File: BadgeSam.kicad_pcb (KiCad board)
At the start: 2 copper layers, 50.1 x 32.4 mm, 2 parts

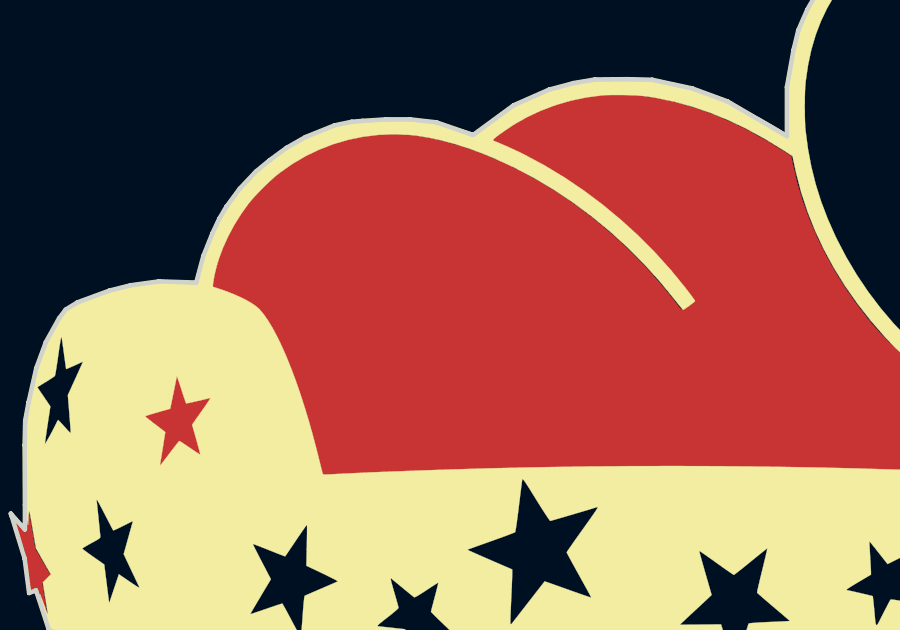
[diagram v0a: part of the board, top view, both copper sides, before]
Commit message: add logo wurth
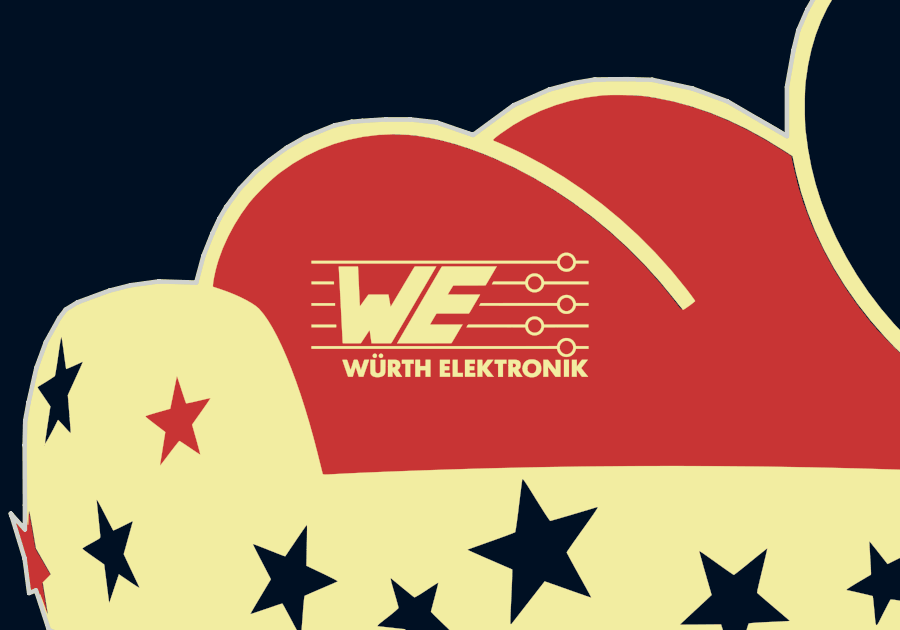
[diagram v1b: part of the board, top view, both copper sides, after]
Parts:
- added G***: LOGO, Aesthetics:wurth_4x4, F.Cu at (132.1, 103.4)

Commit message: define size
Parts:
- added BT1: Battery_Cell, BadgeSam:79523141, B.Cu at (138.9, 117.3)
- added C1: 1uF, Capacitor_SMD:C_0805_2012Metric_Pad1.15x1.40mm_HandSolder, B.Cu at (153.2, 133.3)
- added C2: 0.1uF, Capacitor_SMD:C_0805_2012Metric_Pad1.15x1.40mm_HandSolder, B.Cu at (168.1, 131.3)
- added D1: LED_RGBA, BadgeSam:LED_155124M173200, B.Cu at (118.6, 119.6)
- added D2: LED_RGBA, BadgeSam:LED_155124M173200, B.Cu at (164.3, 97.1)
- added D3: LED_RGBA, BadgeSam:LED_155124M173200, B.Cu at (129.2, 132.4)
- added D4: LED_RGBA, BadgeSam:LED_155124M173200, B.Cu at (153.9, 101.3)
- added R1: 10K, Resistor_SMD:R_0805_2012Metric_Pad1.15x1.40mm_HandSolder, B.Cu at (167.1, 124.0)
- added SW1: RESET, Button_Switch_SMD:SW_SPST_TL3342, B.Cu at (175.6, 114.2)
- added U1: STM8S003F3P, Package_SO:TSSOP-20_4.4x6.5mm_P0.65mm, B.Cu at (160.0, 128.0)
- moved Ref** 106.9 mm to (148.4, 112.4)
- moved G*** 9.26 mm to (130.6, 112.5)
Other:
- board outline removed

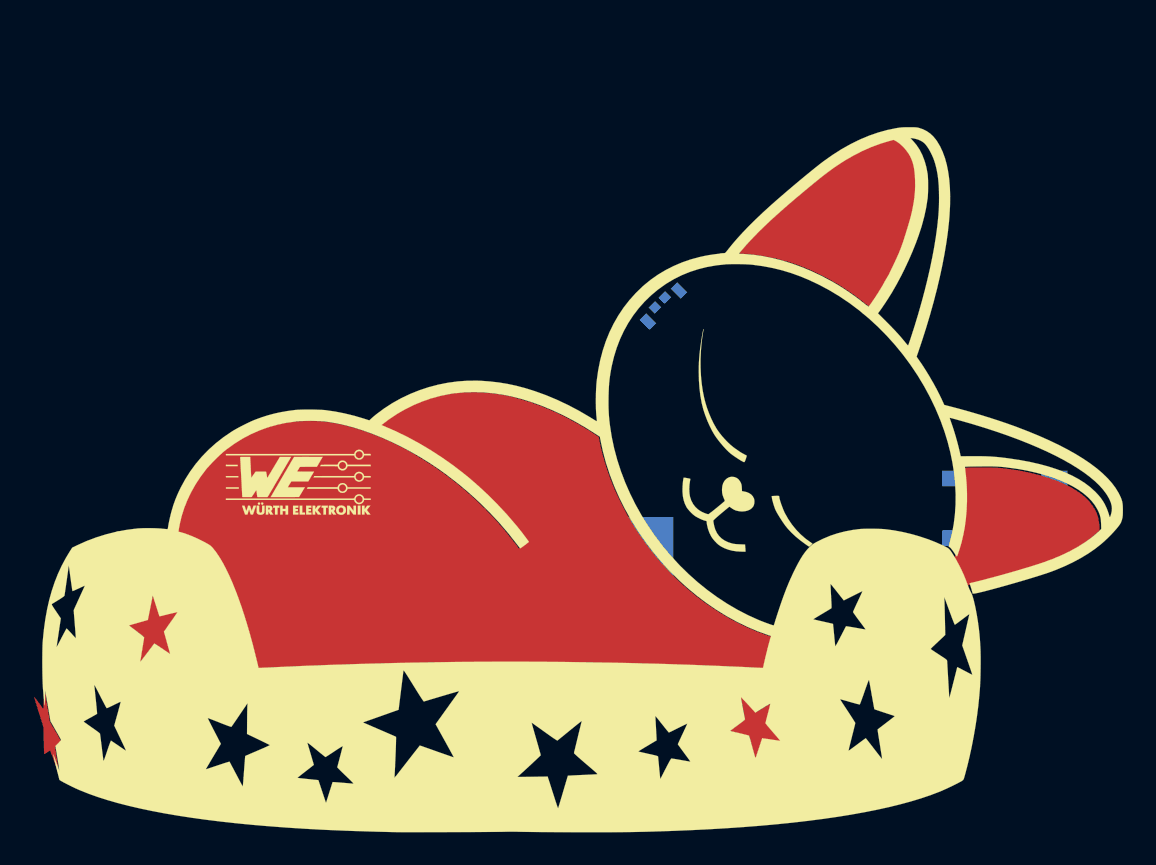
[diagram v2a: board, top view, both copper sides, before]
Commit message: Add EdgeCut and logos
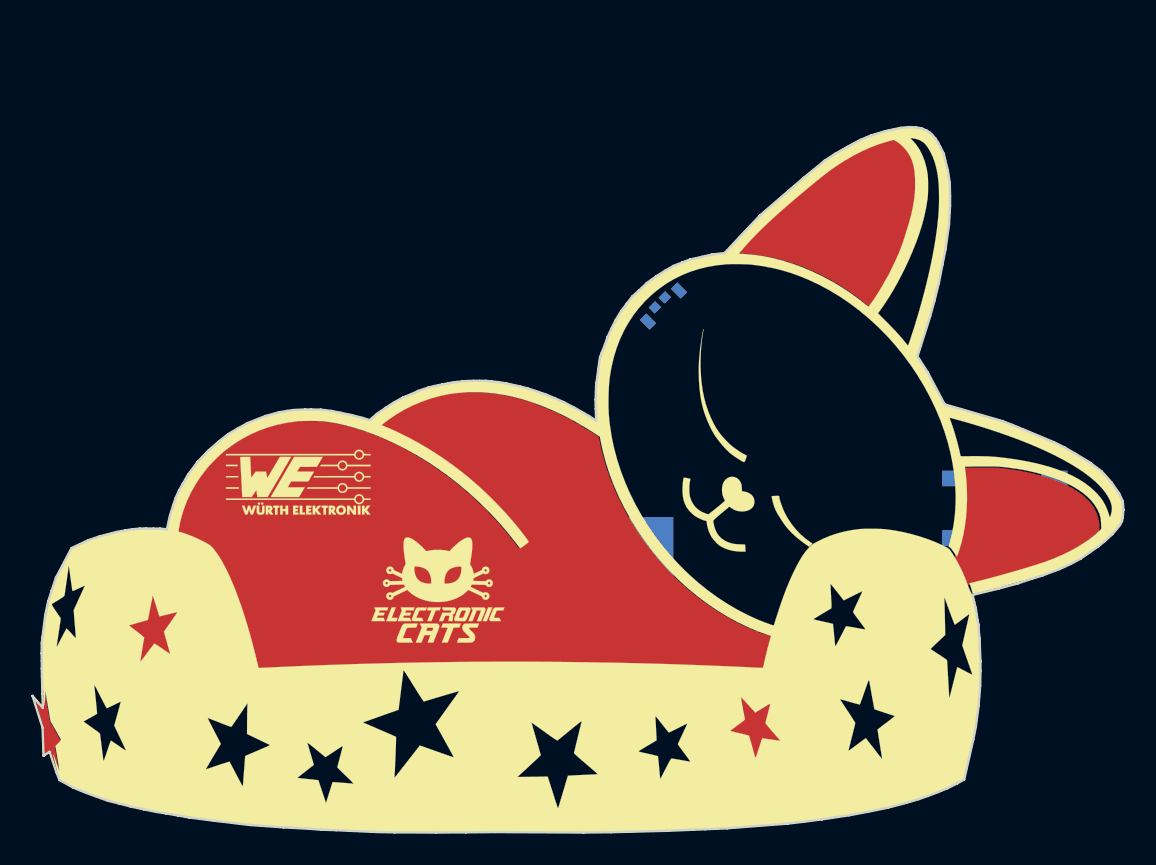
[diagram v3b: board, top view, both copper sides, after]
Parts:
- added G***: LOGO, Aesthetics:electronic_cats_logo_8x6, F.Cu at (139.5, 119.4)
- added G***: LOGO, Aesthetics:electronic_cats_logo_4x3, B.Cu at (123.0, 125.9)
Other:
- board outline added: 69.6 x 45 mm

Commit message: Routeo
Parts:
- moved R1 1.58 mm to (168.7, 123.7)
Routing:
- net +BATT: track 0.00 -> 128.5 mm, vias 0 -> 4
- net GND: track 0.00 -> 85.9 mm, vias 0 -> 7
- net /B3: track 0.00 -> 57.1 mm
- net /R1: track 0.00 -> 54.7 mm, vias 0 -> 2
- net /G1: track 0.00 -> 49.0 mm, vias 0 -> 2
- net /B1: track 0.00 -> 48.5 mm, vias 0 -> 2
- net /G4: track 0.00 -> 35.0 mm
- net /R2: track 0.00 -> 31.9 mm, vias 0 -> 2
- net /G2: track 0.00 -> 31.6 mm, vias 0 -> 2
- net /R4: track 0.00 -> 31.4 mm
- net /B4: track 0.00 -> 30.9 mm
- net /R3: track 0.00 -> 25.7 mm
- net /RST: track 0.00 -> 25.0 mm
- net Net-(C1-Pad1): track 0.00 -> 10.3 mm
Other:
- net class Default: trace_width 0.25 -> 0.3
- net class vcc added: clearance 0.2, trace_width 0.3, via_dia 0.6, via_drill 0.4

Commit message: fix routeo
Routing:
- net /G1: track 49.0 -> 76.2 mm, vias 2 -> 3
- net /B1: track 48.5 -> 71.8 mm, vias 2 -> 4
- net +BATT: track 128.5 -> 137.4 mm, vias 4 -> 3
- net GND: track 85.9 -> 88.5 mm
- net Net-(C1-Pad1): track 10.3 -> 11.7 mm
- net /R1: track 54.7 -> 55.7 mm
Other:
- net class vcc: trace_width 0.3 -> 0.5

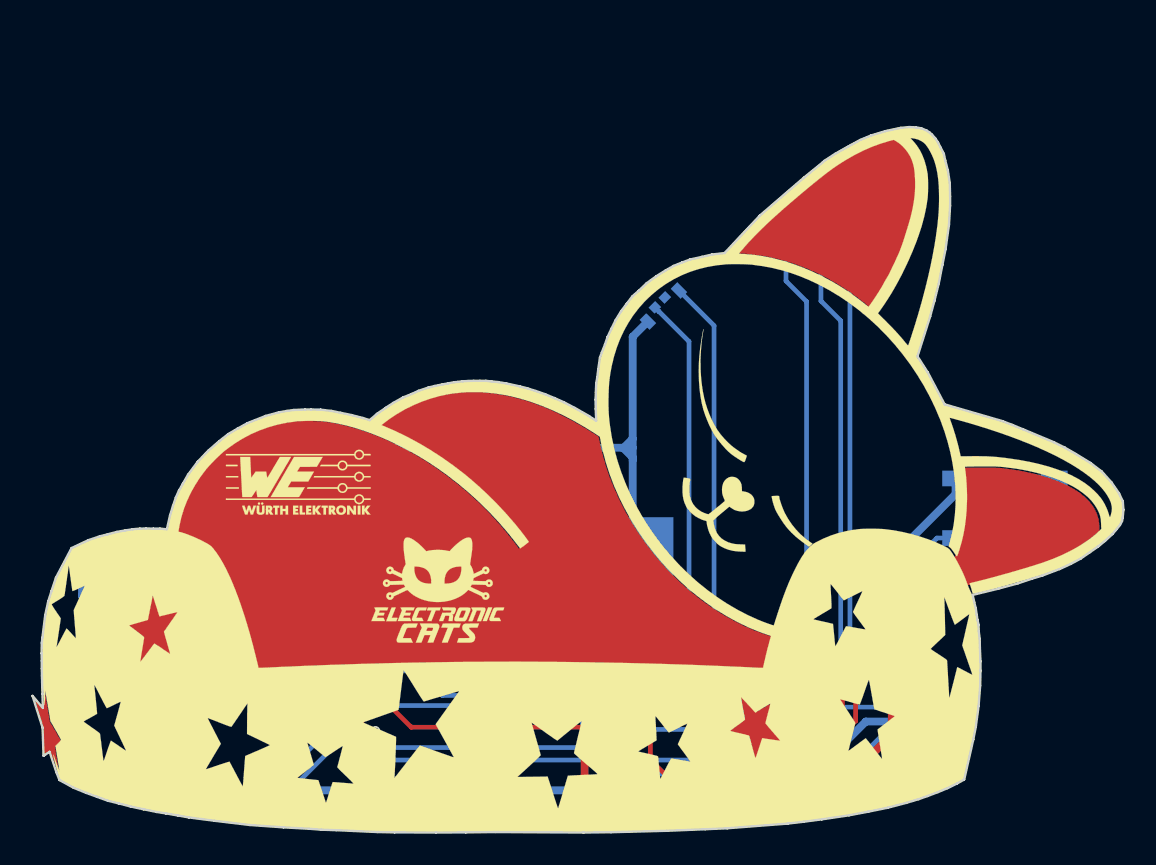
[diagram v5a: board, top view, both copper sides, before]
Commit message: change rgb and footprint led
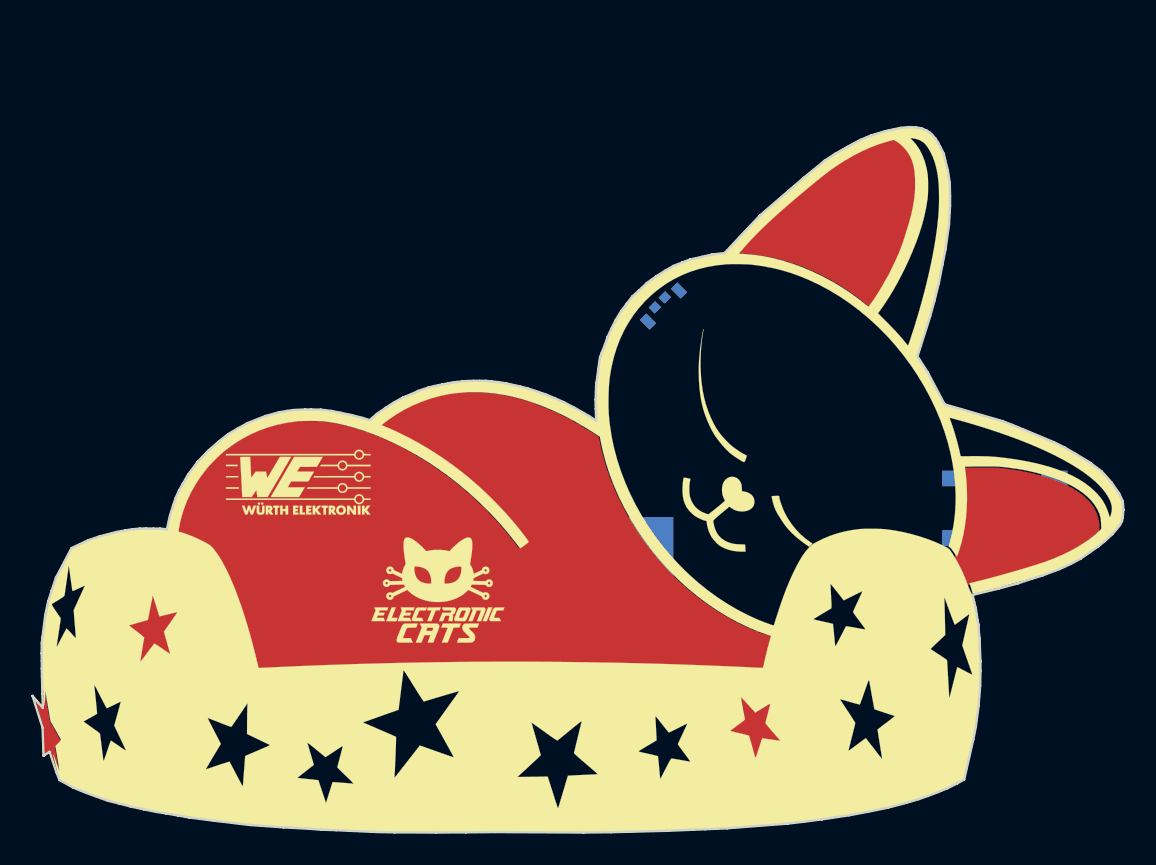
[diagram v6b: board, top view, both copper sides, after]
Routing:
- net +BATT: track 137.4 -> 0.00 mm, vias 3 -> 0
- net GND: track 88.5 -> 0.00 mm, vias 7 -> 0
- net /G1: track 76.2 -> 0.00 mm, vias 3 -> 0
- net /B1: track 71.8 -> 0.00 mm, vias 4 -> 0
- net /B3: track 56.9 -> 0.00 mm
- net /R1: track 55.7 -> 0.00 mm, vias 2 -> 0
- net /G4: track 35.0 -> 0.00 mm
- net /R2: track 32.3 -> 0.00 mm, vias 2 -> 0
- net /G2: track 31.6 -> 0.00 mm, vias 2 -> 0
- net /R4: track 31.4 -> 0.00 mm
- net /B4: track 30.9 -> 0.00 mm
- net /R3: track 25.7 -> 0.00 mm
- net /RST: track 25.0 -> 0.00 mm
- net Net-(C1-Pad1): track 11.7 -> 0.00 mm

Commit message: routeo and pin prog
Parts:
- added J1: PROG, Connector_PinHeader_2.54mm:PinHeader_1x04_P2.54mm_Vertical, B.Cu at (122.1, 130.5)
- D1, D2, D3, D4: value LED_RGBA -> LED_ARGB; footprint BadgeSam:LED_155124M173200 -> BadgeSam:156120M173000
- moved D1 51.9 mm to (170.2, 125.3), turned to 90 degrees
- moved D2 15.8 mm to (165.7, 112.9), turned to 0 degrees
- moved D4 4.86 mm to (158.7, 101.8), turned to 0 degrees
- moved R1 4.38 mm to (169.0, 119.3), turned to 270 degrees
- moved D3 2.44 mm to (129.1, 129.9), turned to 0 degrees
- moved U1 1.69 mm to (160.2, 129.6)
- moved C2 1.03 mm to (167.3, 131.8)
- moved SW1 0.39 mm to (176.0, 114.0)
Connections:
- D1 pad 1: /R1 -> +BATT
- D1 pad 2: /G1 -> /R1
- D1 pad 3: /B1 -> /G1
- D1 pad 4: +BATT -> /B1
- D2 pad 1: /R4 -> +BATT
- D2 pad 2: /G4 -> /R4
- D2 pad 3: /B4 -> /G4
- D2 pad 4: Net-(D2-Pad4) -> /B4
- D3 pad 1: /R2 -> +BATT
- D3 pad 2: /G2 -> /R2
- D3 pad 3: /B3 -> /G2
- D3 pad 4: +BATT -> /B2
- D4 pad 1: /R3 -> +BATT
- D4 pad 2: /G3 -> /R3
- D4 pad 3: /B3 -> /G3
- D4 pad 4: +BATT -> /B3
- U1 pad 14: Net-(U1-Pad14) -> /G3
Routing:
- net +BATT: track 0.00 -> 142.0 mm, vias 0 -> 5
- net GND: track 0.00 -> 114.5 mm, vias 0 -> 5
- net /RST: track 0.00 -> 73.1 mm, vias 0 -> 2
- net /SWIM: track 0.00 -> 37.6 mm, vias 0 -> 2
- net /R2: track 0.00 -> 34.4 mm, vias 0 -> 2
- net /B2: track 0.00 -> 31.1 mm, vias 0 -> 2
- net /G3: track 0.00 -> 30.3 mm
- net /B3: track 0.00 -> 29.7 mm
- net /G2: track 0.00 -> 27.3 mm, vias 0 -> 2
- net /R3: track 0.00 -> 24.2 mm
- net /R4: track 0.00 -> 21.0 mm, vias 0 -> 2
- net /B4: track 0.00 -> 19.4 mm
- net /G1: track 0.00 -> 16.7 mm
- net /G4: track 0.00 -> 15.8 mm
- net /R1: track 0.00 -> 15.4 mm, vias 0 -> 2
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
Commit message: fix track batt
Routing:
- net +BATT: track 142.0 -> 143.2 mm
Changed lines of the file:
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@@
     (thickness 1.6)
     (drawings 228)
-    (tracks 280)
+    (tracks 281)
     (zones 0)
     (modules 16)
@@
   (segment (start 164.19 107.55) (end 164.19 108) (width 0.5) (layer B.Cu) (net 1))
   (segment (start 164.19 108) (end 164.19 112.09) (width 0.5) (layer B.Cu) (net 1))
-  (segment (start 125.988 114.248) (end 125.988 117.348) (width 0.5) (layer B.Cu) (net 1))
-  (segment (start 129.216 111.02) (end 125.988 114.248) (width 0.5) (layer B.Cu) (net 1))
   (segment (start 151.888 114.248) (end 151.888 117.348) (width 0.5) (layer B.Cu) (net 1))
   (segment (start 151.886 111.02) (end 151.888 111.018) (width 0.5) (layer B.Cu) (net 1))
-  (segment (start 148.12 111.02) (end 129.216 111.02) (width 0.5) (layer B.Cu) (net 1))
   (segment (start 151.888 102.562) (end 151.888 106.138) (width 0.5) (layer B.Cu) (net 1))
   (segment (start 153.44 101.01) (end 151.888 102.562) (width 0.5) (layer B.Cu) (net 1))
@@
   (segment (start 151.888 110.508) (end 151.888 111.018) (width 0.5) (layer B.Cu) (net 1))
   (segment (start 151.888 106.138) (end 151.888 110.508) (width 0.5) (layer B.Cu) (net 1))
-  (segment (start 148.12 111.02) (end 150.97 111.02) (width 0.5) (layer B.Cu) (net 1))
   (segment (start 150.97 111.02) (end 151.886 111.02) (width 0.5) (layer B.Cu) (net 1))
   (segment (start 151.376 111.136) (end 151.888 111.648) (width 0.5) (layer B.Cu) (net 1))
@@
   (segment (start 169.03 118.28) (end 169 118.31) (width 0.5) (layer B.Cu) (net 1))
   (segment (start 170.82 118.28) (end 169.03 118.28) (width 0.5) (layer B.Cu) (net 1))
+  (segment (start 127.12 111.02) (end 125.988 112.152) (width 0.5) (layer B.Cu) (net 1))
+  (segment (start 125.988 112.152) (end 125.988 117.348) (width 0.5) (layer B.Cu) (net 1))
+  (segment (start 150.97 111.02) (end 127.12 111.02) (width 0.5) (layer B.Cu) (net 1))
   (segment (start 179.13 112.08) (end 172.83 112.08) (width 0.5) (layer B.Cu) (net 2))
   (segment (start 138.95 132.68) (end 139.6 133.33) (width 0.5) (layer B.Cu) (net 2))
@@
   (segment (start 137.84 133.66) (end 137.86 133.68) (width 0.3) (layer B.Cu) (net 15))
   (segment (start 128.07 133.66) (end 137.84 133.66) (width 0.3) (layer B.Cu) (net 15))
-  (via (at 161.06 129.74) (size 0.6) (drill 0.4) (layers F.Cu B.Cu) (net 15))
-  (segment (start 162.13 128.67) (end 161.06 129.74) (width 0.3) (layer B.Cu) (net 15))
   (segment (start 163.19 128.67) (end 162.13 128.67) (width 0.3) (layer B.Cu) (net 15))
-  (segment (start 161.06 130.814185) (end 161.06 130.164264) (width 0.3) (layer F.Cu) (net 15))
-  (segment (start 161.06 130.164264) (end 161.06 129.74) (width 0.3) (layer F.Cu) (net 15))
   (segment (start 137.86 133.68) (end 158.582002 133.68) (width 0.3) (layer F.Cu) (net 15))
   (segment (start 160.086597 132.175405) (end 160.086597 131.787588) (width 0.3) (layer F.Cu) (net 15))
   (segment (start 158.582002 133.68) (end 160.086597 132.175405) (width 0.3) (layer F.Cu) (net 15))
   (segment (start 160.086597 131.787588) (end 161.06 130.814185) (width 0.3) (layer F.Cu) (net 15))
+  (segment (start 161.06 130.814185) (end 161.435815 130.814185) (width 0.3) (layer F.Cu) (net 15))
+  (via (at 161.87 129.76) (size 0.6) (drill 0.4) (layers F.Cu B.Cu) (net 15))
+  (segment (start 161.87 130.38) (end 161.87 129.76) (width 0.3) (layer F.Cu) (net 15))
+  (segment (start 161.435815 130.814185) (end 161.87 130.38) (width 0.3) (layer F.Cu) (net 15))
+  (segment (start 161.87 128.93) (end 162.13 128.67) (width 0.3) (layer B.Cu) (net 15))
+  (segment (start 161.87 129.76) (end 161.87 128.93) (width 0.3) (layer B.Cu) (net 15))
   (segment (start 157.29 132.57) (end 155.83 132.57) (width 0.3) (layer B.Cu) (net 16))
   (segment (start 134.41 129.08) (end 130.66 129.08) (width 0.3) (layer B.Cu) (net 16))
